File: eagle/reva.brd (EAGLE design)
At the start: 89 x 55 mm, 232 parts, among them IC1 LM555D, IC2 74HC174D, J1 TYPE-C-31-M-12, U1 TPS63002DRCR

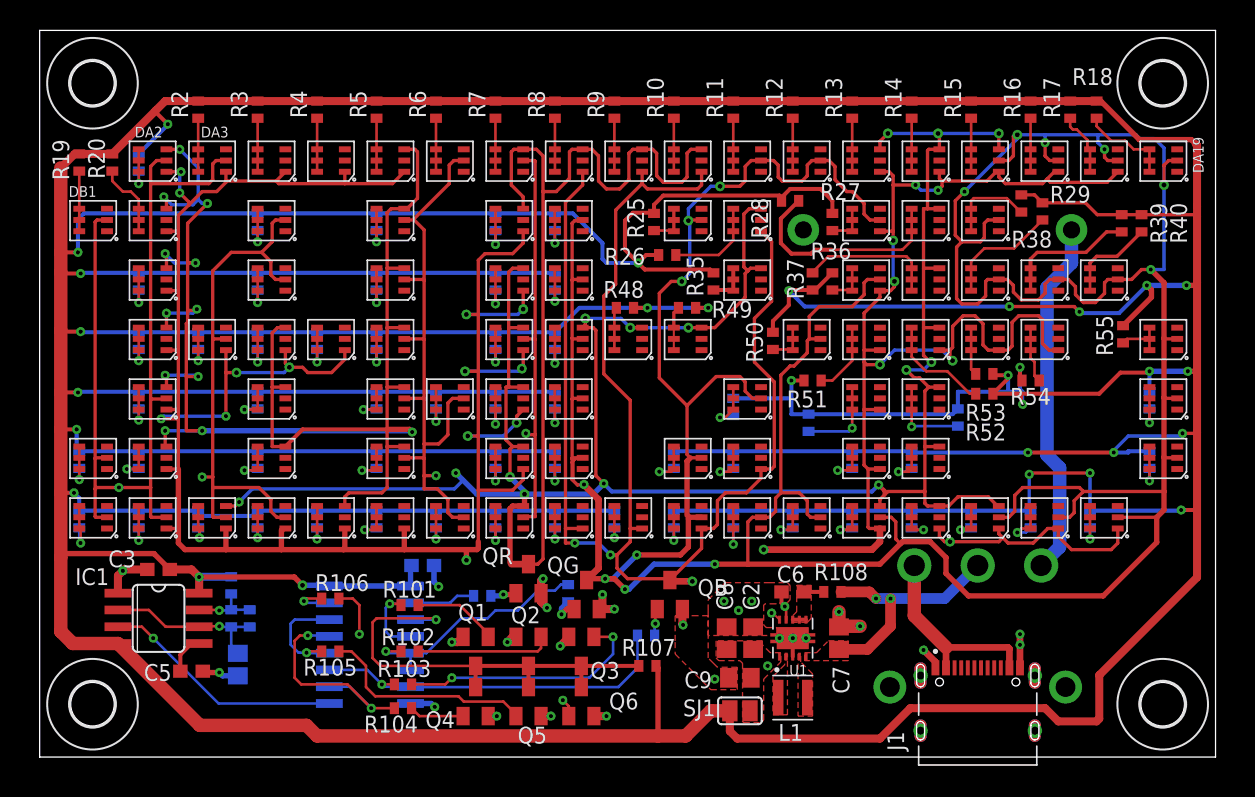
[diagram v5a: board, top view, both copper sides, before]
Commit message: Change buck to have 20uF Cout, increase inductor footprint size
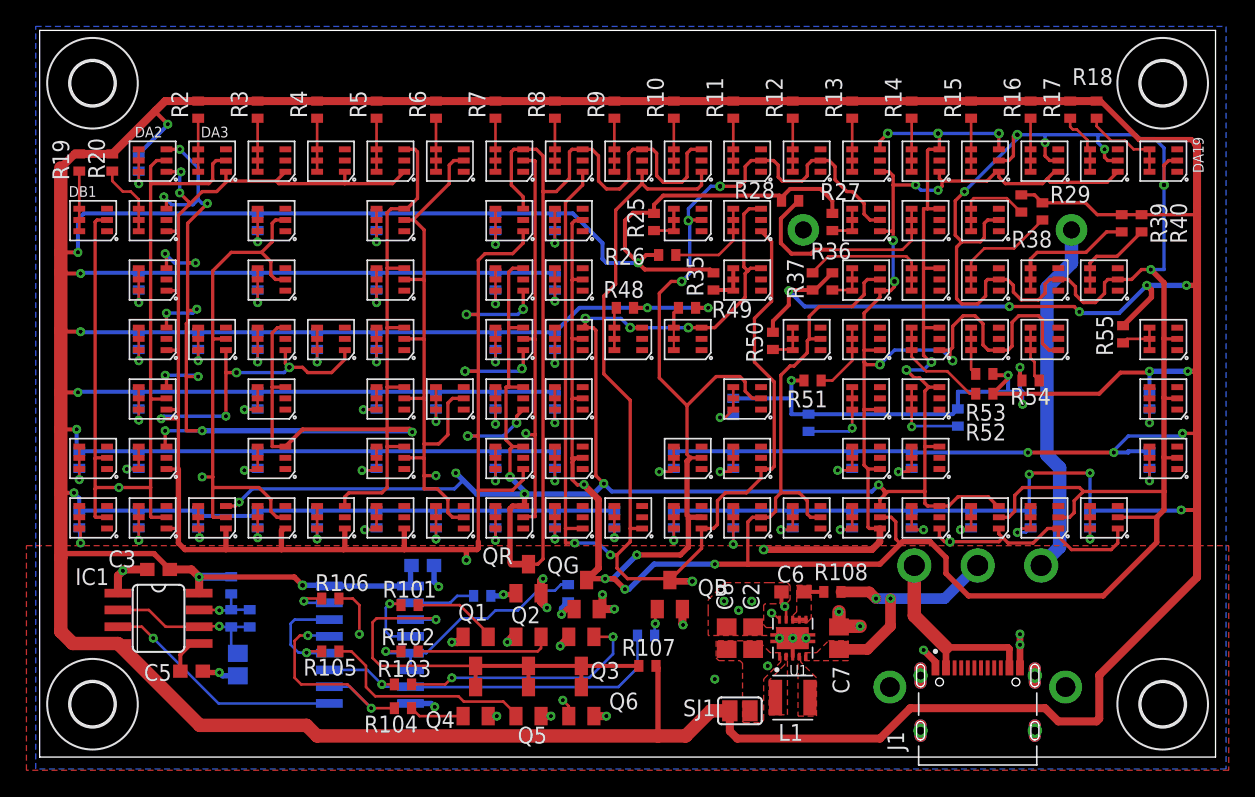
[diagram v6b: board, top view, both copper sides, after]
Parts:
- removed C9: 10u, adafruit:C0805
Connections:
- net N$100 renamed L1
- net N$101 renamed L2
- net 5VBUCK: no longer C9.1
- net GND: no longer C9.2
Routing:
- added copper zone on layer 16, net GND
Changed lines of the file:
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@@
 <layers>
 <layer number="1" name="Top" color="4" fill="1" visible="yes" active="yes"/>
-<layer number="2" name="Route2" color="16" fill="1" visible="yes" active="yes"/>
+<layer number="2" name="Route2" color="16" fill="1" visible="no" active="yes"/>
 <layer number="3" name="Route3" color="17" fill="1" visible="no" active="no"/>
 <layer number="4" name="Route4" color="18" fill="1" visible="no" active="no"/>
@@
 <layer number="13" name="Route13" color="21" fill="1" visible="no" active="no"/>
 <layer number="14" name="Route14" color="22" fill="1" visible="no" active="no"/>
-<layer number="15" name="Route15" color="23" fill="1" visible="yes" active="yes"/>
-<layer number="16" name="Bottom" color="1" fill="1" visible="yes" active="yes"/>
+<layer number="15" name="Route15" color="23" fill="1" visible="no" active="yes"/>
+<layer number="16" name="Bottom" color="1" fill="1" visible="no" active="yes"/>
 <layer number="17" name="Pads" color="2" fill="1" visible="yes" active="yes"/>
 <layer number="18" name="Vias" color="2" fill="1" visible="yes" active="yes"/>
@@
 <layer number="20" name="Dimension" color="24" fill="1" visible="yes" active="yes"/>
 <layer number="21" name="tPlace" color="7" fill="1" visible="yes" active="yes"/>
-<layer number="22" name="bPlace" color="7" fill="1" visible="yes" active="yes"/>
+<layer number="22" name="bPlace" color="7" fill="1" visible="no" active="yes"/>
 <layer number="23" name="tOrigins" color="15" fill="1" visible="yes" active="yes"/>
-<layer number="24" name="bOrigins" color="15" fill="1" visible="yes" active="yes"/>
+<layer number="24" name="bOrigins" color="15" fill="1" visible="no" active="yes"/>
 <layer number="25" name="tNames" color="7" fill="1" visible="yes" active="yes"/>
-<layer number="26" name="bNames" color="7" fill="1" visible="yes" active="yes"/>
+<layer number="26" name="bNames" color="7" fill="1" visible="no" active="yes"/>
 <layer number="27" name="tValues" color="7" fill="1" visible="no" active="yes"/>
 <layer number="28" name="bValues" color="7" fill="1" visible="no" active="yes"/>
@@
 <layer number="38" name="bTest" color="7" fill="1" visible="no" active="yes"/>
 <layer number="39" name="tKeepout" color="4" fill="11" visible="yes" active="yes"/>
-<layer number="40" name="bKeepout" color="1" fill="11" visible="yes" active="yes"/>
+<layer number="40" name="bKeepout" color="1" fill="11" visible="no" active="yes"/>
 <layer number="41" name="tRestrict" color="4" fill="10" visible="yes" active="yes"/>
-<layer number="42" name="bRestrict" color="1" fill="10" visible="yes" active="yes"/>
+<layer number="42" name="bRestrict" color="1" fill="10" visible="no" active="yes"/>
 <layer number="43" name="vRestrict" color="2" fill="10" visible="no" active="yes"/>
 <layer number="44" name="Drills" color="7" fill="1" visible="no" active="yes"/>
@@
 <layer number="50" name="dxf" color="7" fill="1" visible="no" active="yes"/>
 <layer number="51" name="tDocu" color="7" fill="1" visible="yes" active="yes"/>
-<layer number="52" name="bDocu" color="7" fill="1" visible="yes" active="yes"/>
+<layer number="52" name="bDocu" color="7" fill="1" visible="no" active="yes"/>
 <layer number="53" name="tGND_GNDA" color="7" fill="9" visible="no" active="no"/>
 <layer number="54" name="bGND_GNDA" color="1" fill="9" visible="no" active="no"/>
@@
 </element>
 <element name="R28" library="adafruit" library_urn="urn:adsk.eagle:library:420" package="R0402" package3d_urn="urn:adsk.eagle:package:6240564/1" value="" x="56.8" y="42.1" smashed="yes" rot="R180">
-<attribute name="NAME" x="53.862" y="42.335" size="1.27" layer="25" rot="R270"/>
+<attribute name="NAME" x="52.565" y="42.262" size="1.27" layer="25"/>
 <attribute name="VALUE" x="57.435" y="44.132" size="1.27" layer="27" rot="R180"/>
 </element>
@@
 <attribute name="VALUE" x="54.286" y="8.111" size="1.27" layer="27" rot="R90"/>
 </element>
-<element name="C9" library="adafruit" library_urn="urn:adsk.eagle:library:420" package="C0805" package3d_urn="urn:adsk.eagle:package:6240337/1" value="10u" x="53" y="6" smashed="yes" rot="R180">
-<attribute name="NAME" x="50.889" y="6.484" size="1.27" layer="25" rot="R180"/>
-<attribute name="VALUE" x="53.889" y="8.286" size="1.27" layer="27" rot="R180"/>
-</element>
 <element name="SJ1" library="jumper" library_urn="urn:adsk.eagle:library:252" package="SJ" package3d_urn="urn:adsk.eagle:package:15471/1" value="" x="53" y="3.5" smashed="yes" rot="R180">
 <attribute name="NAME" x="51.151" y="4.357" size="1.27" layer="25" ratio="10" rot="R180"/>
@@
 <contactref element="C2" pad="2"/>
 <contactref element="C8" pad="2"/>
-<contactref element="C9" pad="2"/>
 <via x="56" y="9" extent="1-16" drill="0.3" diameter="0.45"/>
 <via x="57" y="9" extent="1-16" drill="0.3" diameter="0.45"/>
@@
 <vertex x="55.8" y="9.8"/>
 </polygon>
-<polygon width="0.1524" layer="1" thermals="no">
-<vertex x="50.6" y="10.7"/>
-<vertex x="49.8" y="10.7"/>
-<vertex x="48.1" y="10.7"/>
-<vertex x="48.1" y="8.7"/>
-<vertex x="48.1" y="7.8"/>
-<vertex x="50.8" y="5.1"/>
-<vertex x="52.8" y="5.1"/>
-<vertex x="52.8" y="6.8"/>
-<vertex x="51.3" y="6.8"/>
-<vertex x="51" y="7.1"/>
-<vertex x="50.6" y="7.5"/>
-<vertex x="50.6" y="9.1"/>
-</polygon>
 <via x="51.8" y="11.8" extent="1-16" drill="0.3" diameter="0.5"/>
 <via x="53.9" y="11.8" extent="1-16" drill="0.3" diameter="0.5"/>
@@
 <via x="51.1" y="5.9" extent="1-16" drill="0.3" diameter="0.5"/>
 <contactref element="BAT1" pad="NEG"/>
+<polygon width="0.1524" layer="16">
+<vertex x="-0.3" y="55.3"/>
+<vertex x="89.8" y="55.3"/>
+<vertex x="89.8" y="-0.9"/>
+<vertex x="-0.3" y="-0.9"/>
+</polygon>
+<polygon width="0.1524" layer="1" rank="6">
+<vertex x="-1" y="-1"/>
+<vertex x="-1" y="16"/>
+<vertex x="90" y="16"/>
+<vertex x="90" y="-1"/>
+</polygon>
 </signal>
 <signal name="CLK_1HZ">
@@
 <wire x1="25.5" y1="10.5" x2="29.9" y2="10.5" width="0.2" layer="1"/>
 </signal>
-<signal name="N$100">
+<signal name="L1">
 <contactref element="U1" pad="4"/>
 <contactref element="L1" pad="1"/>
@@
 <vertex x="57.4" y="7.8"/>
 <vertex x="57.4" y="3.1"/>
-<vertex x="58.5" y="3.1"/>
-<vertex x="58.5" y="6.3"/>
+<vertex x="58.8" y="3.1"/>
+<vertex x="58.8" y="6"/>
 <vertex x="57.6" y="7.2"/>
 <vertex x="57.6" y="7.8"/>
 </polygon>
 </signal>
-<signal name="N$101">
+<signal name="L2">
 <contactref element="U1" pad="2"/>
 <contactref element="L1" pad="2"/>
@@
 <vertex x="56.4" y="7.8"/>
 <vertex x="56.4" y="7"/>
-<vertex x="55.5" y="6.1"/>
-<vertex x="55.5" y="3.2"/>
+<vertex x="55.2" y="5.8"/>
+<vertex x="55.2" y="3.2"/>
 <vertex x="56.6" y="3.2"/>
 <vertex x="56.6" y="7.8"/>
@@
 <contactref element="U1" pad="10"/>
 <contactref element="U1" pad="1"/>
-<contactref element="C9" pad="1"/>
 <contactref element="C8" pad="1"/>
 <contactref element="C2" pad="1"/>

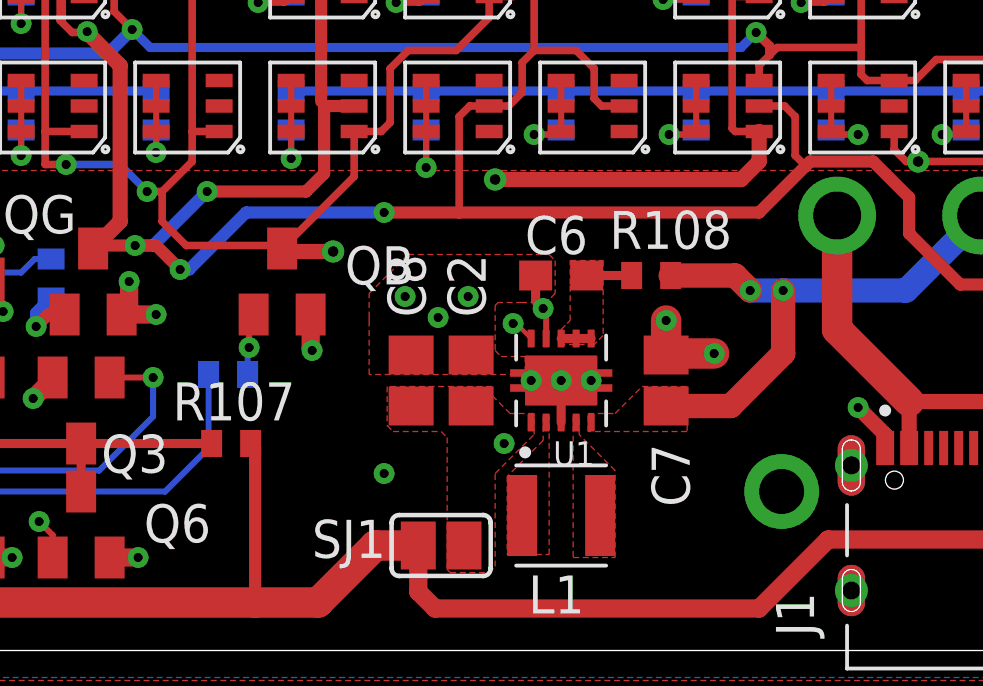
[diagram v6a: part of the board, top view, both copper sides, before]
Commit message: Add resistive feedback to TP63000
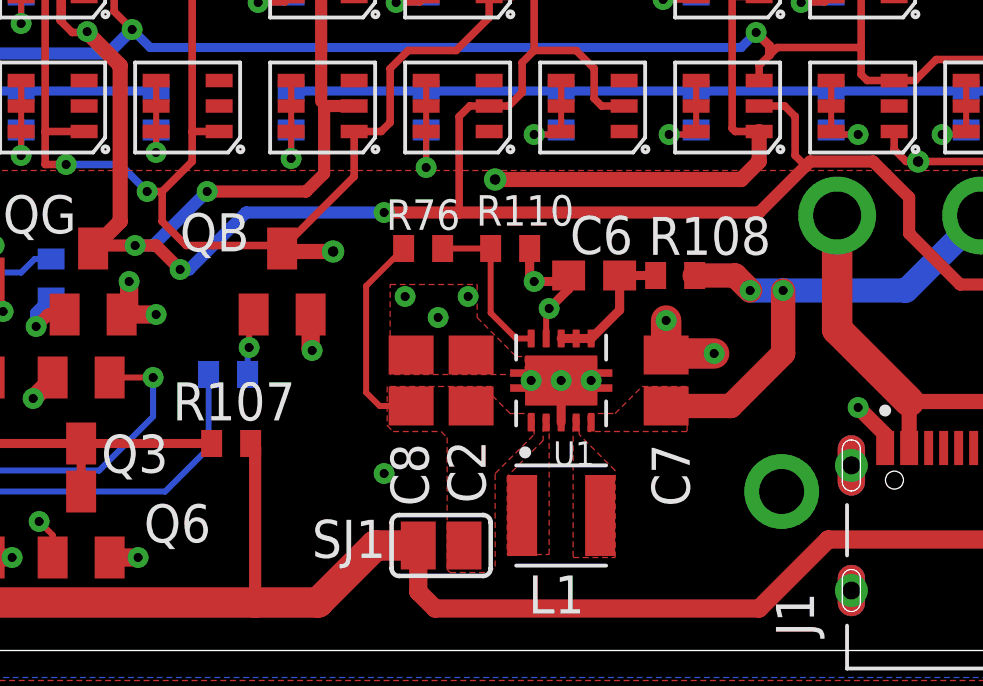
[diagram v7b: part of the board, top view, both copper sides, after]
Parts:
- added R110: 75k, adafruit:R0402
- added R76: 680k, adafruit:R0402
- moved C6 1.10 mm to (58.1, 12.5)
- moved R108 0.80 mm to (60.8, 12.5)
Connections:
- new net N$76: R110.2, R76.1, U1.10
- net 5VBUCK: now also R76.2; no longer U1.10
- net GND: now also R110.1
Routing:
- net N$76: track 0.00 -> 5.45 mm
- net GND: track 32.2 -> 34.7 mm, vias 28 -> 29
- net VINA: track 2.50 -> 4.69 mm
- net 5VBUCK: track 4.93 -> 7.00 mm, vias 2 -> 0
- net BUCK_IN: track 18.3 -> 17.5 mm
- removed copper zone on layer 1, net VINA
